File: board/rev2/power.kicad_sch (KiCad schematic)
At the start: 16 parts, among them J1 USB_C_Receptacle_USB2.0_14P, J2 Screw_Terminal_01x02, U8 TPS62933F

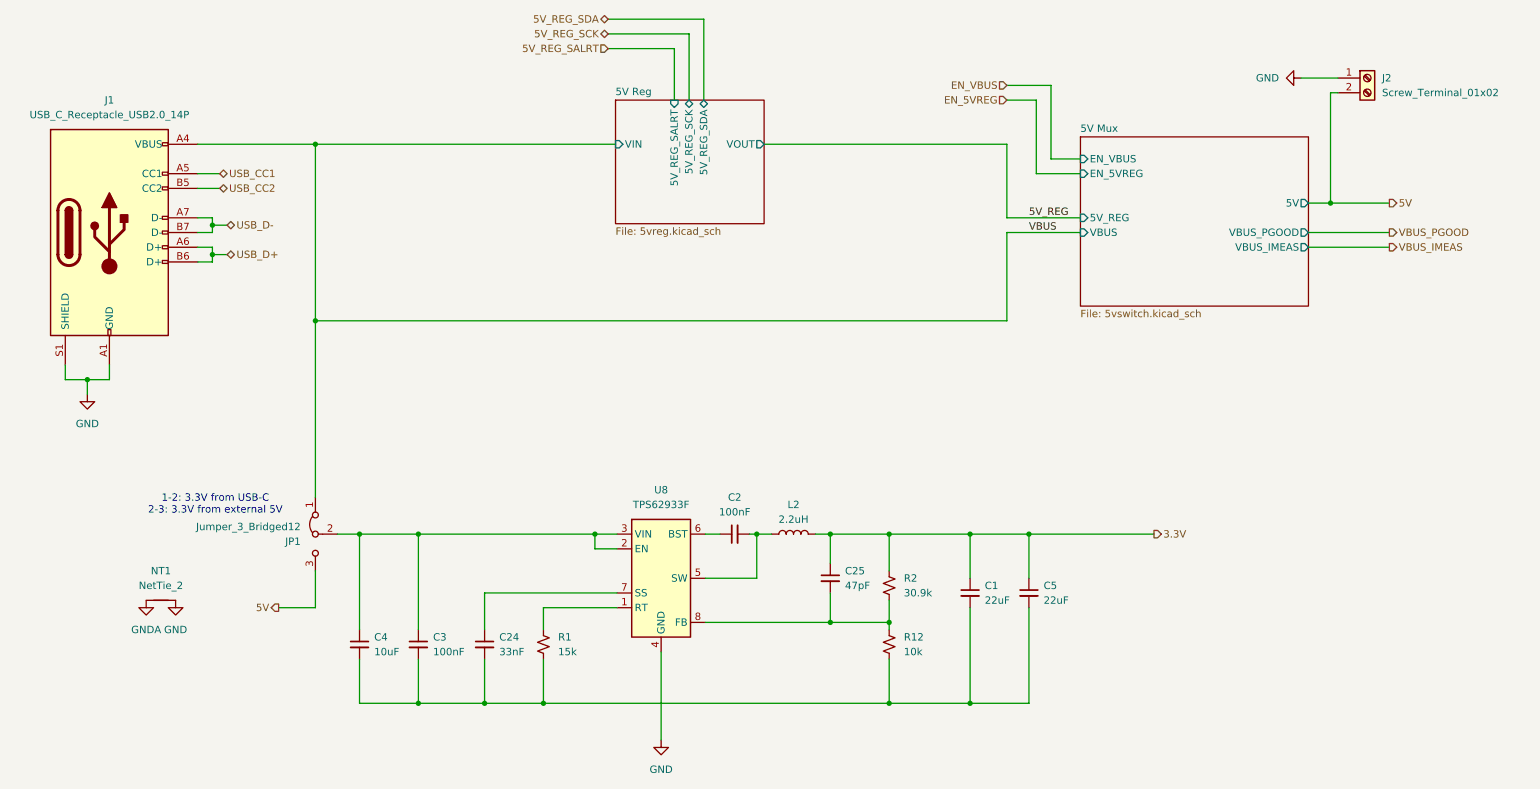
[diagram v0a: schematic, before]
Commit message: Continue board work
- move to rp2040, separate stm32g071 to do usb-c + aux ctrl IO
  - still cheaper lol with the cost of stm32s
- more power reg stuff
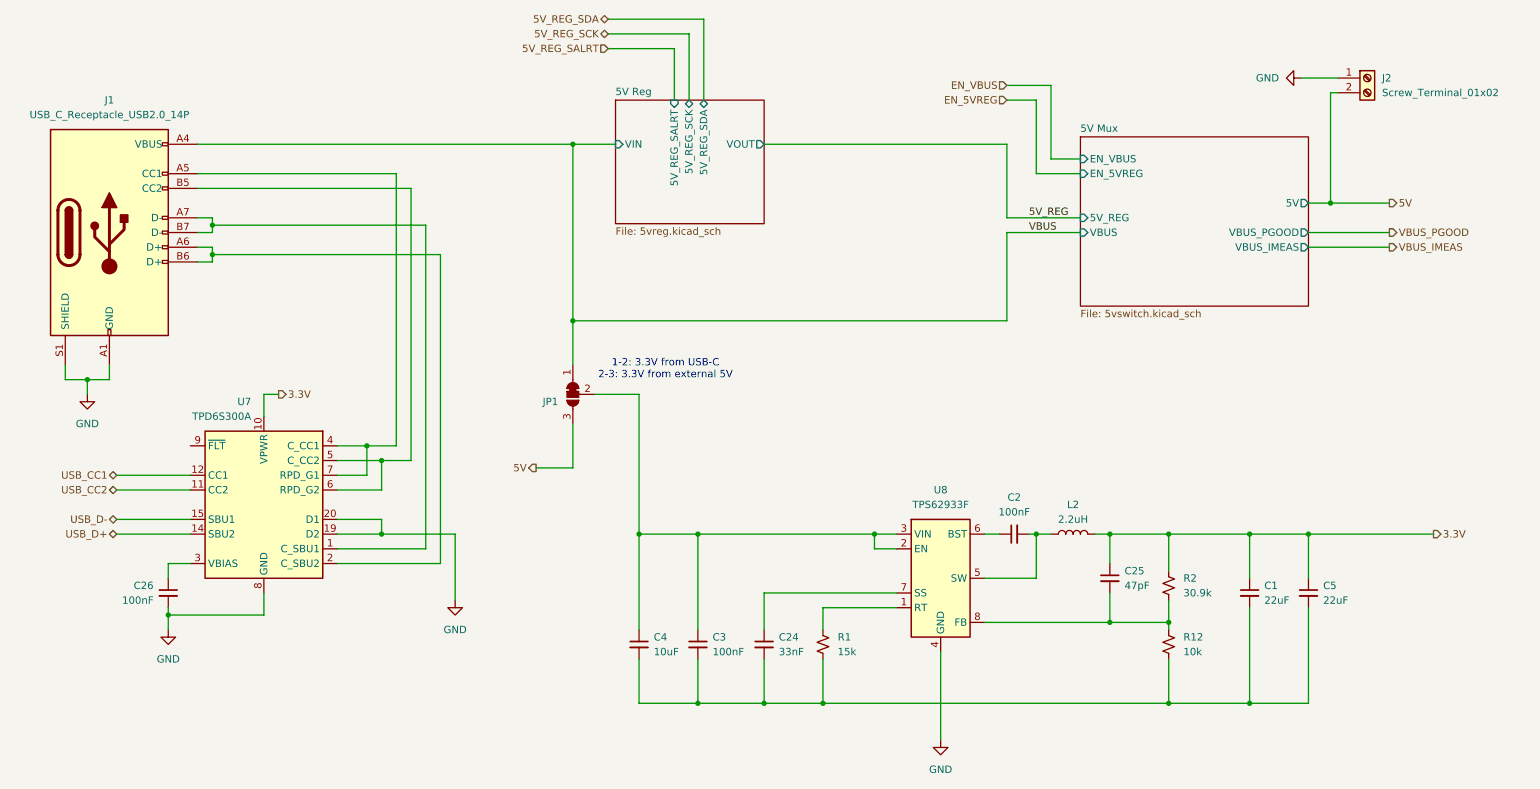
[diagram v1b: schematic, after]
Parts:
- removed JP1: Jumper_3_Bridged12, symbol Jumper:Jumper_3_Bridged12
- removed NT1: NetTie_2, symbol Device:NetTie_2
- added C26: 100nF, symbol Device:C_Small
- added JP1: SolderJumper_3_Bridged12, symbol Jumper:SolderJumper_3_Bridged12
- added U7: TPD6S300A, Package_DFN_QFN:WQFN-20-1EP_3x3mm_P0.4mm_EP1.7x1.7mm_ThermalVias, symbol Power_Protection:TPD6S300A
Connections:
- net 3.3V: now also U7.10 (VPWR)
- net 5V: now also JP1.3 (B)
- net GND: now also C26.2, U7.13 (GND), U7.16 (GND), U7.17 (GND), U7.18 (GND), U7.19 (D2), U7.20 (D1), U7.21 (GND), U7.8 (GND)
- net USB_CC1: now also U7.12 (CC1); no longer J1.A5 (CC1)
- net USB_CC2: now also U7.11 (CC2); no longer J1.B5 (CC2)
- net USB_D+: now also U7.14 (SBU2); no longer J1.A6 (D+), J1.B6 (D+)
- net USB_D-: now also U7.15 (SBU1); no longer J1.A7 (D-), J1.B7 (D-)
- net VBUS: now also JP1.1 (A)
- net at C3.1, C4.1, U8.2 (EN)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: now also JP1.2 (C)
- new net: J1.A5 (CC1), U7.4 (C_CC1), U7.7 (RPD_G1)
- new net: J1.A6 (D+), J1.B6 (D+), U7.2 (C_SBU2)
- new net: J1.A7 (D-), J1.B7 (D-), U7.1 (C_SBU1)
- new net: J1.B5 (CC2), U7.5 (C_CC2), U7.6 (RPD_G2)
- new net: C26.1, U7.3 (VBIAS)
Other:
- moved on the sheet: C1, C2, C24, C25, C3, C4, C5, L2, R1, R12, R2, U8

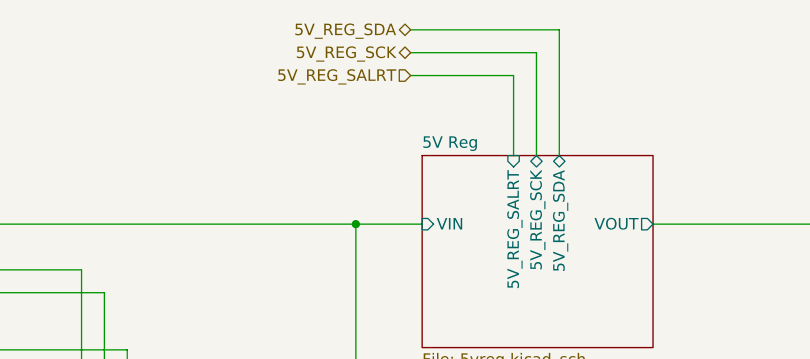
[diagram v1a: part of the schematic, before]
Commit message: Split out board into A/B
allow 2x displays (for chaining)
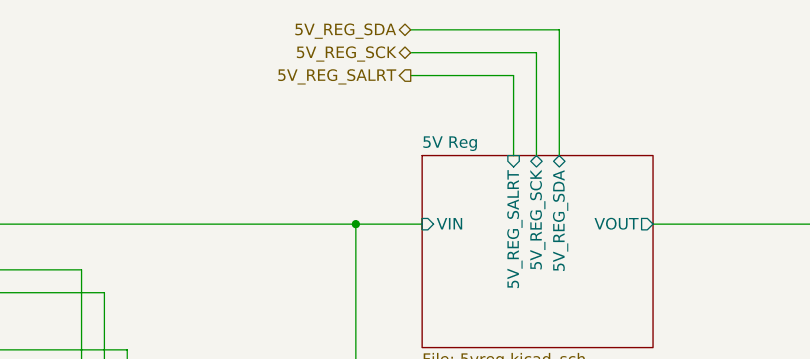
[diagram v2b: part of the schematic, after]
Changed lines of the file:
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@@
 	)
 	(hierarchical_label "5V_REG_SALRT"
-		(shape input)
+		(shape output)
 		(at 125.476 34.29 180)
 		(effects
@@
 			(project "mainboard"
 				(path "/32eb05c7-b4a6-42f3-8fb3-43453631100f/802d77e5-f72d-443e-abfe-d20b44acef6c"
-					(page "5")
-				)
-			)
+					(page "4")
+				)
+			)

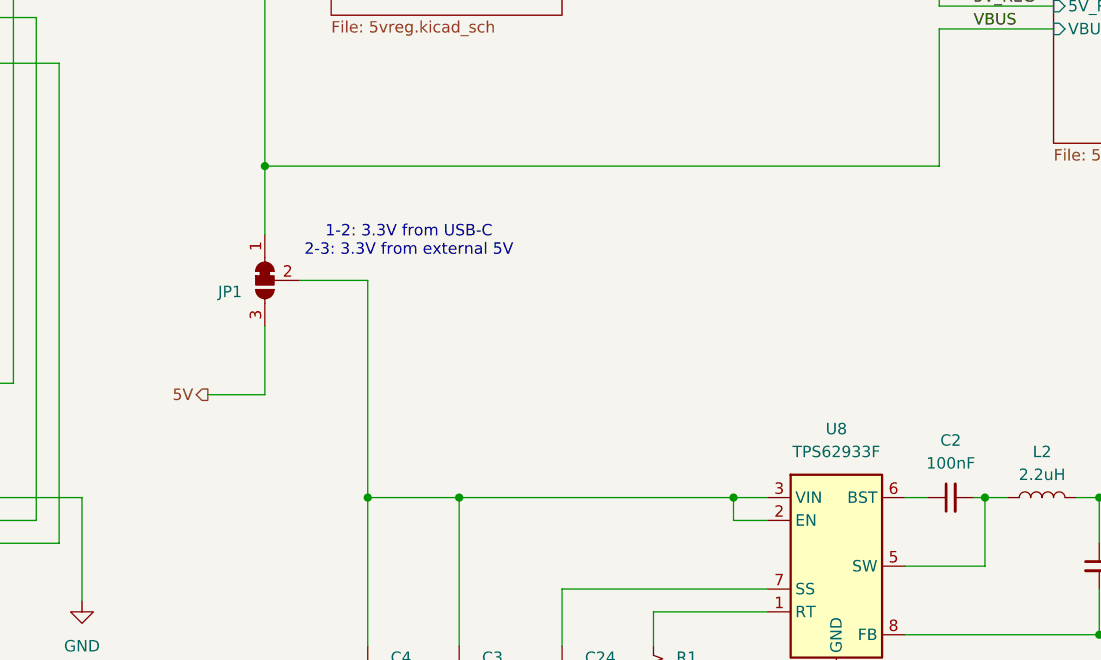
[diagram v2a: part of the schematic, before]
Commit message: Board GPIO allocation
- and usbmux

still need to do termination on the big buses + a bunch of bypass caps
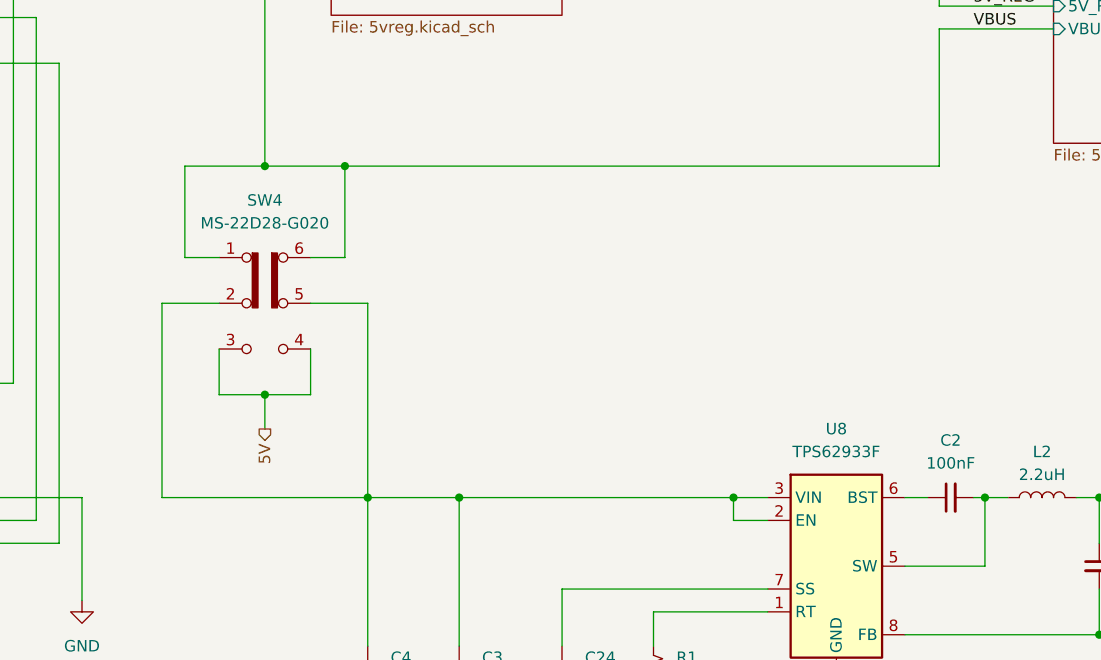
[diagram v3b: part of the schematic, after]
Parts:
- removed JP1: SolderJumper_3_Bridged12, symbol Jumper:SolderJumper_3_Bridged12
- added SW4: MS-22D28-G020, symbol Switch:SW_Slide_DPDT
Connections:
- net 5V: now also SW4.3 (C), SW4.4 (A)
- net VBUS: now also SW4.1 (A), SW4.6 (C)
- net at C3.1, C4.1, U8.2 (EN)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: now also SW4.2 (B), SW4.5 (B)
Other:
- note removed: "1-2: 3.3V from USB-C 2-3: 3.3V from external 5V"
- company: (none) -> MLABS
- title: (none) -> Power Supply (3.3V)

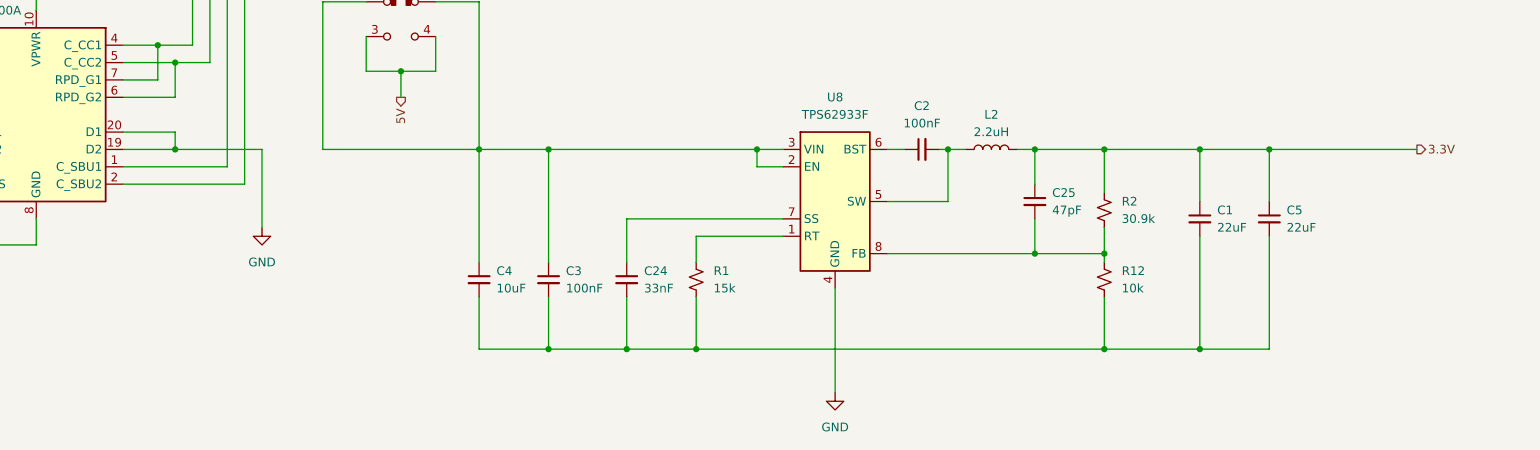
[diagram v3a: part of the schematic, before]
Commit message: Continue board, assign caps/res, adjust for JLC availability
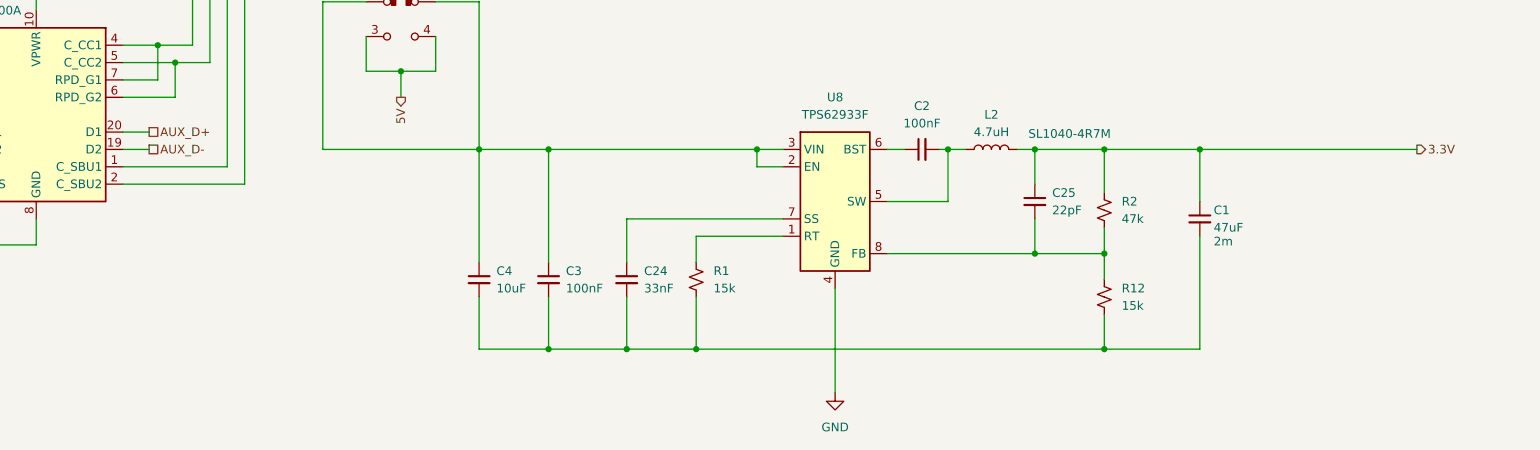
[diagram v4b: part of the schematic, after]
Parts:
- removed C5: 22uF, symbol Device:C_Small
- C1: value 22uF -> 47uF; footprint (none) -> Capacitor_SMD:C_1206_3216Metric; ESR (none) -> 2m; Part (none) -> CL31A476MPHNNNE
- C2, C26, C3: footprint (none) -> Capacitor_SMD:C_0402_1005Metric; Part (none) -> CL05B104KB54PNC
- C24: footprint (none) -> Capacitor_SMD:C_0603_1608Metric; Part (none) -> CL10B333KB8NNNC
- C25: value 47pF -> 22pF; footprint (none) -> Capacitor_SMD:C_0402_1005Metric; Part (none) -> 0402CG220J500NT
- C4: footprint (none) -> Capacitor_SMD:C_1210_3225Metric; Part (none) -> CL31A106KBHNNNE
- J2: footprint (none) -> TerminalBlock_TE-Connectivity:TerminalBlock_TE_282834-2_1x02_P2.54mm_Horizontal
- L2: value 2.2uH -> 4.7uH; footprint (none) -> Inductor_SMD:L_TechFuse_SL1040; Part (none) -> SL1040-4R7M
- R1: footprint (none) -> Resistor_SMD:R_0805_2012Metric; Part (none) -> 0805W8F1502T5E
- R12: value 10k -> 15k; footprint (none) -> Resistor_SMD:R_0805_2012Metric; Part (none) -> 0805W8F1502T5E
- R2: value 30.9k -> 47k; footprint (none) -> Resistor_SMD:R_0805_2012Metric; Part (none) -> 0805W8F4702T5E
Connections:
- net GND: no longer U7.19 (D2), U7.20 (D1)
- new net AUX_D+: U7.20 (D1)
- new net AUX_D-: U7.19 (D2)
